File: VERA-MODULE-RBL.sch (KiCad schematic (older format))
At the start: 14 parts

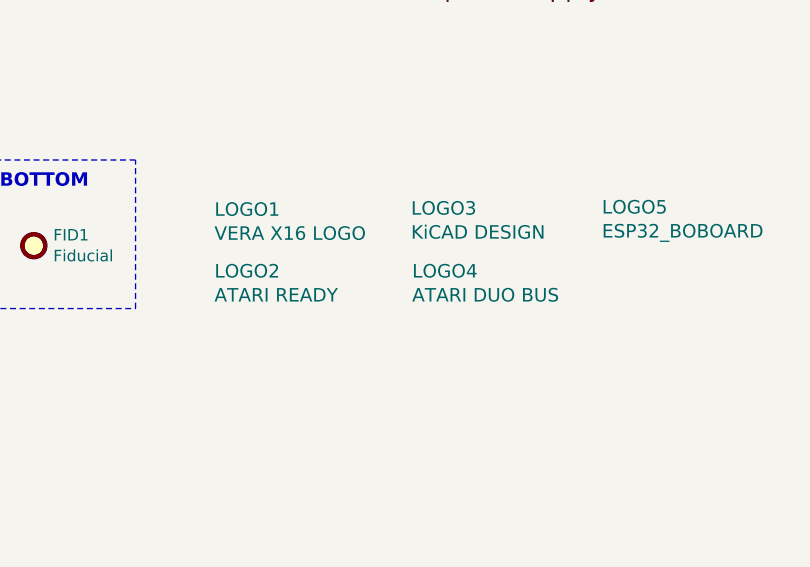
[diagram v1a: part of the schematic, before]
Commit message: Remove leftover Atari content from the C64 project
- VERA-ATARI-HW-REQUIREMENTS.md renamed VERA-C64-HW-REQUIREMENTS.md,
  references updated (analysis PDF rebuilt)
- LOGO2 "ATARI READY" becomes "C64 READY" (c64_ready_8mm_REV); LOGO4
  "ATARI DUO BUS" (DUOCart bus logo) removed from schematic and netlist
- VERA-MODULE-RBL.csv regenerated from the current netlist (it still
  listed the Atari CART1/ECI1 of October 2025)
- stale Atari exports removed: VERA-MODULE-RBL.xml and the *.sch-bak
  backups, now ignored

What still says Atari on purpose: provenance notes (derived from
RBL-XE) and the PCB with its production files, still the Atari layout
until it is updated from the netlist.
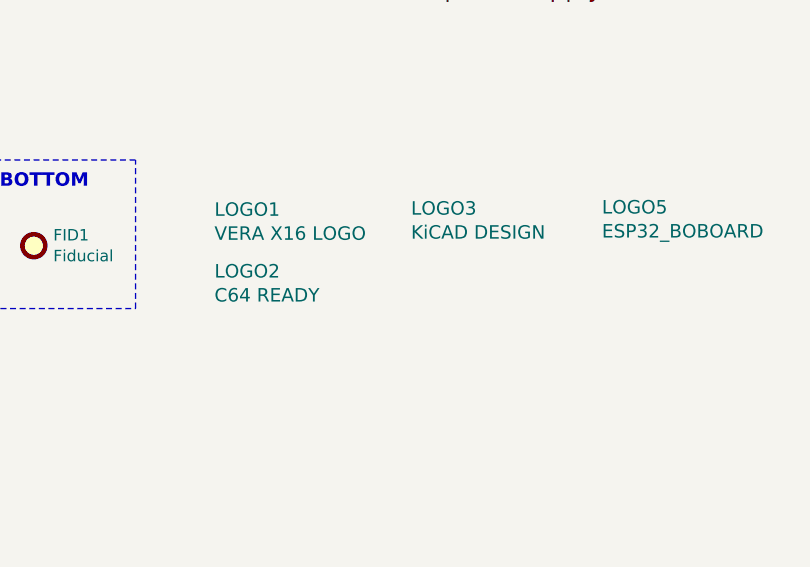
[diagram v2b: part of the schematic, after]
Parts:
- removed LOGO4: ATARI DUO BUS, RetroBitLab:DUOCart_20x11_Rev, symbol RetroBitLab:LOGO
- LOGO2: value ATARI READY -> C64 READY; footprint RetroBitLab:atari_ready_8mm_rev -> RetroBitLab:c64_ready_8mm_REV
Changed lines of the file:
@@
 P 3930 6300
 F 0 "LOGO2" H 3955 6353 59  0000 L CNN
-F 1 "ATARI READY" H 3955 6248 59  0000 L CNN
-F 2 "RetroBitLab:atari_ready_8mm_rev" H 3930 6300 59  0001 C CNN
+F 1 "C64 READY" H 3955 6248 59  0000 L CNN
+F 2 "RetroBitLab:c64_ready_8mm_REV" H 3930 6300 59  0001 C CNN
 F 3 "" H 3930 6300 59  0001 C CNN
 	1    3930 6300
@@
 	1    0    0    -1
 $EndComp
-$Comp
-L RetroBitLab:LOGO LOGO4
-U 1 1 68C454BC
-P 4795 6300
-F 0 "LOGO4" H 4820 6353 59  0000 L CNN
-F 1 "ATARI DUO BUS" H 4820 6248 59  0000 L CNN
-F 2 "RetroBitLab:DUOCart_20x11_Rev" H 4795 6300 59  0001 C CNN
-F 3 "" H 4795 6300 59  0001 C CNN
-	1    4795 6300
-	1    0    0    -1
-$EndComp
